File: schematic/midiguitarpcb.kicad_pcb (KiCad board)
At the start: 2 copper layers, 50 x 50 mm, 37 parts, among them CN1 NMJ6HCD2, J1 USB_C_Receptacle_USB2.0_16P, SW1 SW_Omron_B3FS, U1 AMS1117-3.3, U2 DIN-504D-M5, U3 STM32H743ZITx

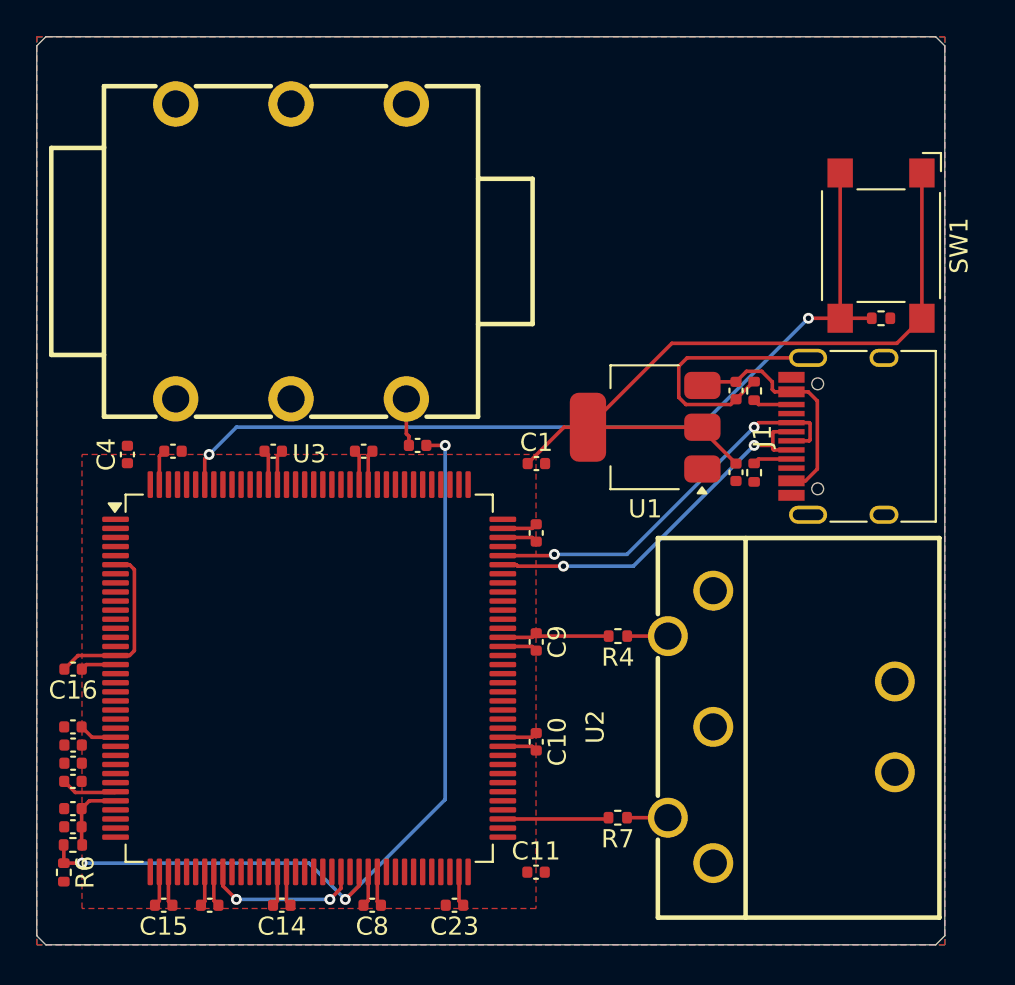
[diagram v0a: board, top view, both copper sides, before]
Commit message: wip working but noisy
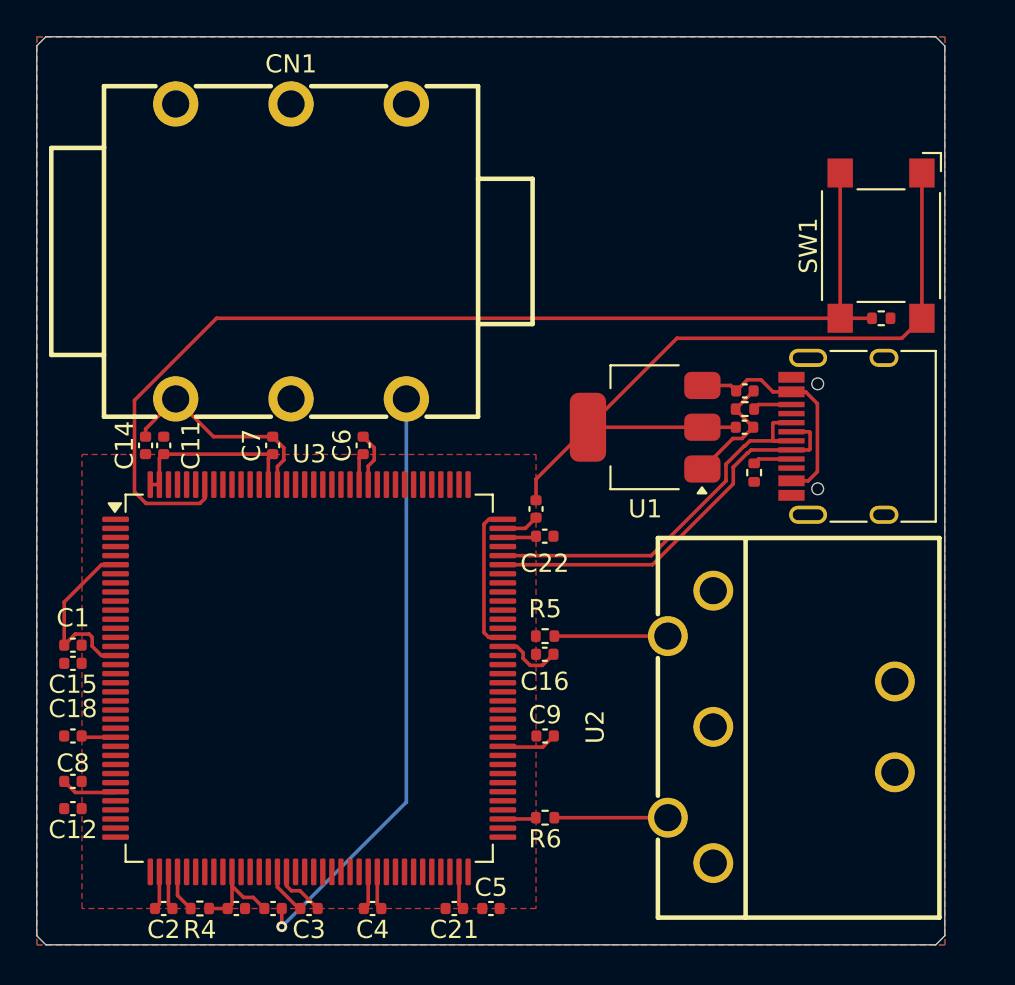
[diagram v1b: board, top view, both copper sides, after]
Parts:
- removed C23, C24: 2.2uF, Capacitor_SMD:C_0402_1005Metric
- removed R7: 10, Resistor_SMD:R_0402_1005Metric
- C19: value 47pF -> 1uF
- C20: value 100nF -> 100pF
- C21: value 1uF -> 2.2uF
- C22: value 100nF -> 2.2uF
- R4: value 33 -> 100K
- R5: value 100K -> 33
- R6: value 100K -> 10
- moved C11 31.2 mm to (57.0, 72.5), turned to 90 degrees
- moved C5 30.7 mm to (75.0, 98.0)
- moved R5 28.4 mm to (78.0, 83.0), turned to 180 degrees
- moved C4 28.4 mm to (68.5, 98.0), turned to 180 degrees
- moved R4 27.5 mm to (59.0, 98.0)
- moved C1 27.4 mm to (52.0, 83.5), turned to 180 degrees
- moved R6 26.7 mm to (78.0, 93.0), turned to 180 degrees
- moved C14 26.4 mm to (56.0, 72.5), turned to 90 degrees
- moved C16 26.0 mm to (78.0, 84.0), turned to 0 degrees
- moved C21 21.5 mm to (73.0, 98.0)
- moved C8 17.8 mm to (52.0, 91.0)
- moved C3 15.8 mm to (65.0, 98.0)
- moved C15 14.2 mm to (52.0, 84.5)
- moved C10 12.8 mm to (77.5, 76.0)
- moved C20 10.5 mm to (61.0, 98.0)
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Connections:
- C19 pad 1: Net-(U3-PA7) -> Net-(U3-PB0)
- C19 pad 2: Net-(U3-PC4) -> Net-(CN1-T)
- C20 pad 1: Net-(U3-VREF+) -> GND
- C20 pad 2: GND -> Net-(U3-PB0)
- C21 pad 1: Net-(U3-VREF+) -> Net-(C21-Pad1)
- C22 pad 1: Net-(CN1-T) -> Net-(C22-Pad1)
- C22 pad 2: Net-(U3-PE9) -> GND
- R4 pad 1: Net-(R4-Pad1) -> Net-(U3-PB0)
- R4 pad 2: +3V3 -> Net-(U3-PA4)
- R5 pad 1: Net-(U3-PE9) -> Net-(R5-Pad1)
- R5 pad 2: Net-(U3-VREF+) -> +3V3
- R6 pad 1: Net-(U3-PE9) -> Net-(R6-Pad1)
- R6 pad 2: GND -> Net-(U3-PB14)
- U2 pad 4: Net-(R4-Pad1) -> Net-(R5-Pad1)
- U2 pad 5: Net-(R7-Pad1) -> Net-(R6-Pad1)
- U3 pad 106: Net-(C24-Pad1) -> Net-(C22-Pad1)
- U3 pad 32: Net-(U3-VREF+) -> unconnected-(U3-VREF+-Pad32)
- U3 pad 40: unconnected-(U3-PA4-Pad40) -> Net-(U3-PA4)
- U3 pad 43: Net-(U3-PA7) -> unconnected-(U3-PA7-Pad43)
- U3 pad 44: Net-(U3-PC4) -> unconnected-(U3-PC4-Pad44)
- U3 pad 45: Net-(U3-PC5) -> unconnected-(U3-PC5-Pad45)
- U3 pad 46: unconnected-(U3-PB0-Pad46) -> Net-(U3-PB0)
- U3 pad 58: Net-(U3-PC5) -> unconnected-(U3-PE7-Pad58)
- U3 pad 60: Net-(U3-PE9) -> unconnected-(U3-PE9-Pad60)
- U3 pad 71: Net-(C23-Pad1) -> Net-(C21-Pad1)
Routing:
- net Net-(U3-PE9): track 47.5 -> 0.00 mm, vias 3 -> 0
- net Net-(CN1-T): track 2.62 -> 32.9 mm, vias 0 -> 1
- net Net-(U3-BOOT0): track 49.4 -> 60.5 mm, vias 2 -> 0
- net Net-(U3-PC5): track 8.74 -> 0.00 mm, vias 2 -> 0
- net GND: track 42.3 -> 50.2 mm
- net Net-(R6-Pad1): track 0.00 -> 6.25 mm
- net Net-(R5-Pad1): track 0.00 -> 6.25 mm
- net Net-(U3-PB0): track 0.00 -> 6.20 mm
- net +3V3: track 63.6 -> 69.5 mm
- net Net-(U3-VREF+): track 4.06 -> 0.00 mm
- net Net-(U3-PB14): track 5.85 -> 1.85 mm
- net Net-(U3-PA4): track 0.00 -> 2.32 mm
- net Net-(R7-Pad1): track 2.25 -> 0.00 mm
- net Net-(R4-Pad1): track 2.24 -> 0.00 mm
- net Net-(C21-Pad1): track 0.00 -> 2.11 mm
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
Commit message: redo pcb
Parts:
- added FB1: FerriteBead, Inductor_SMD:L_0805_2012Metric, F.Cu at (56.9, 23.0)
- added FB2: FerriteBead, Inductor_SMD:L_0805_2012Metric, F.Cu at (87.0, 33.5)
- added FB3: FerriteBead, Inductor_SMD:L_0805_2012Metric, F.Cu at (87.0, 43.5)
- added R7: 100K, Resistor_SMD:R_0805_2012Metric, F.Cu at (42.9, 36.0)
- added R8: 100K, Resistor_SMD:R_0805_2012Metric, F.Cu at (50.9, 36.0)
- added R9: 0, Resistor_SMD:R_0805_2012Metric, F.Cu at (63.9, 27.0)
- C1, C4, C9: value 100nF -> 1uF; footprint Capacitor_SMD:C_0402_1005Metric -> Capacitor_SMD:C_0805_2012Metric
- C10: value 100nF -> 10uF; footprint Capacitor_SMD:C_0402_1005Metric -> Capacitor_SMD:C_0805_2012Metric
- C11: value 100nF -> 100pF; footprint Capacitor_SMD:C_0402_1005Metric -> Capacitor_SMD:C_0805_2012Metric
- C12: value 4.7uF -> 100nF; footprint Capacitor_SMD:C_0402_1005Metric -> Capacitor_SMD:C_0805_2012Metric
- C13: value 10uF -> 1uF; footprint Capacitor_SMD:C_0402_1005Metric -> Capacitor_SMD:C_0805_2012Metric
- C14, C16: value 100nF -> 2.2uF; footprint Capacitor_SMD:C_0402_1005Metric -> Capacitor_SMD:C_0805_2012Metric
- C15, C18, C2, C3, C5, C6, C7: footprint Capacitor_SMD:C_0402_1005Metric -> Capacitor_SMD:C_0805_2012Metric
- C17: value 10uF -> 100nF; footprint Capacitor_SMD:C_0402_1005Metric -> Capacitor_SMD:C_0805_2012Metric
- C19: value 1uF -> 100nF; footprint Capacitor_SMD:C_0402_1005Metric -> Capacitor_SMD:C_0805_2012Metric
- C20: value 100pF -> 100nF; footprint Capacitor_SMD:C_0402_1005Metric -> Capacitor_SMD:C_0805_2012Metric
- C21: value 2.2uF -> 100nF; footprint Capacitor_SMD:C_0402_1005Metric -> Capacitor_SMD:C_0805_2012Metric
- C22: value 2.2uF -> 4.7uF; footprint Capacitor_SMD:C_0402_1005Metric -> Capacitor_SMD:C_0805_2012Metric
- C8: value 1uF -> 10uF; footprint Capacitor_SMD:C_0402_1005Metric -> Capacitor_SMD:C_0805_2012Metric
- R1: value 10K -> 33; footprint Resistor_SMD:R_0402_1005Metric -> Resistor_SMD:R_0805_2012Metric
- R2: value 5.1K -> 10K; footprint Resistor_SMD:R_0402_1005Metric -> Resistor_SMD:R_0805_2012Metric
- R3: value 5.1K -> 10; footprint Resistor_SMD:R_0402_1005Metric -> Resistor_SMD:R_0805_2012Metric
- R4: value 100K -> 5.1K; footprint Resistor_SMD:R_0402_1005Metric -> Resistor_SMD:R_0805_2012Metric
- R5: value 33 -> 5.1K; footprint Resistor_SMD:R_0402_1005Metric -> Resistor_SMD:R_0805_2012Metric
- R6: value 10 -> 100K; footprint Resistor_SMD:R_0402_1005Metric -> Resistor_SMD:R_0805_2012Metric
- U1: value AMS1117-3.3 -> DIN-504D-M5; footprint Package_TO_SOT_SMD:SOT-223-3_TabPin2 -> din5:CONN-TH_DIN-504D-M5
- U2: value DIN-504D-M5 -> STM32H743VGTx; footprint din5:CONN-TH_DIN-504D-M5 -> Package_QFP:LQFP-100_14x14mm_P0.5mm
- U3: value STM32H743ZITx -> AMS1117-3.3; footprint Package_QFP:LQFP-144_20x20mm_P0.5mm -> Package_TO_SOT_SMD:SOT-223-3_TabPin2
- moved R4 85.0 mm to (94.0, 20.5)
- moved C8 78.5 mm to (90.3, 22.5), turned to 0 degrees
- moved C12 74.2 mm to (77.9, 23.0)
- moved C4 73.5 mm to (60.4, 25.0), turned to 0 degrees
- moved C3 73.0 mm to (64.0, 25.0)
- moved C5 72.5 mm to (60.4, 27.0)
- moved C21 71.2 mm to (67.4, 27.0)
- moved C2 71.0 mm to (56.9, 27.0)
- moved C20 69.4 mm to (71.9, 29.5), turned to 0 degrees
- moved C19 69.1 mm to (53.9, 29.5)
- moved U3 65.4 mm to (84.2, 22.8), turned to 180 degrees
- moved R6 64.0 mm to (48.9, 36.0), turned to -90 degrees
- moved C9 62.1 mm to (44.9, 36.0), turned to 90 degrees
- moved R5 61.1 mm to (93.9, 24.0)
- moved C1 58.7 mm to (56.9, 25.0)
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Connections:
- C1 pad 1: +3V3 -> Net-(U2-VDDA)
- C1 pad 2: GND -> GNDA
- C11 pad 1: +3V3 -> Net-(U2-PC4)
- C11 pad 2: GND -> Net-(U2-PA7)
- C13 pad 1: VBUS -> Net-(CN1-T)
- C13 pad 2: GND -> Net-(U2-PC5)
- C14 pad 1: +3V3 -> Net-(C14-Pad1)
- C16 pad 1: +3V3 -> Net-(C16-Pad1)
- C18 pad 1: Net-(U3-NRST) -> +3V3
- C19 pad 1: Net-(U3-PB0) -> +3V3
- C19 pad 2: Net-(CN1-T) -> GND
- C2 pad 1: +3V3 -> Net-(U2-VDDA)
- C2 pad 2: GND -> GNDA
- C20 pad 1: GND -> +3V3
- C20 pad 2: Net-(U3-PB0) -> GND
- C21 pad 1: Net-(C21-Pad1) -> +3V3
- C22 pad 1: Net-(C22-Pad1) -> +3V3
- C3 pad 1: +3V3 -> GND
- C3 pad 2: GND -> Net-(U2-NRST)
- C4 pad 1: +3V3 -> VDDA
- C4 pad 2: GND -> GNDA
- C5 pad 1: +3V3 -> VDDA
- C5 pad 2: GND -> GNDA
- C6 pad 1: +3V3 -> Net-(U3-VI)
- C7 pad 1: +3V3 -> Net-(U2-PB0)
- C7 pad 2: GND -> GNDA
- C8 pad 1: +3V3 -> Net-(U3-VI)
- C9 pad 1: +3V3 -> Net-(U2-PB0)
- C9 pad 2: GND -> GNDA
- CN1 pad 3: GND -> GNDA
- CN1 pad 4: GND -> GNDA
- J1 pad A4: VBUS -> Net-(U3-VI)
- J1 pad A6: Net-(U3-PA12) -> Net-(U2-PA11)
- J1 pad A7: Net-(U3-PA11) -> Net-(U2-PA10)
- J1 pad A9: VBUS -> Net-(U3-VI)
- J1 pad B4: VBUS -> Net-(U3-VI)
- J1 pad B6: Net-(U3-PA12) -> Net-(U2-PA11)
- J1 pad B7: Net-(U3-PA11) -> Net-(U2-PA10)
- J1 pad B9: VBUS -> Net-(U3-VI)
- R1 pad 1: Net-(U3-BOOT0) -> Net-(FB2-Pad1)
- R1 pad 2: GND -> +3V3
- R2 pad 1: Net-(J1-CC2) -> Net-(U2-BOOT0)
- R3 pad 1: Net-(J1-CC1) -> Net-(FB3-Pad1)
- R3 pad 2: GND -> Net-(U2-PA9)
- R4 pad 1: Net-(U3-PB0) -> Net-(J1-CC2)
- R4 pad 2: Net-(U3-PA4) -> GND
- R5 pad 1: Net-(R5-Pad1) -> Net-(J1-CC1)
- R5 pad 2: +3V3 -> GND
- R6 pad 1: Net-(R6-Pad1) -> VDDA
- R6 pad 2: Net-(U3-PB14) -> Net-(U2-PB0)
- SW1 pad 2: Net-(U3-BOOT0) -> Net-(U2-BOOT0)
- U1 pad 1: GND -> unconnected-(U1-Pad1)
- U1 pad 2: +3V3 -> GND
- U1 pad 3: VBUS -> unconnected-(U1-Pad3)
- U2 pad 2: GND -> unconnected-(U2-PE3-Pad2)
- U2 pad 4: Net-(R5-Pad1) -> unconnected-(U2-PE5-Pad4)
- U2 pad 5: Net-(R6-Pad1) -> unconnected-(U2-PE6-Pad5)
- U2 pad 6: GND -> +3V3
- U2 pad 7: GND -> unconnected-(U2-PC13-Pad7)
- U3 pad 1: unconnected-(U3-PE2-Pad1) -> GND
- U3 pad 2: unconnected-(U3-PE3-Pad2) -> +3V3
- U3 pad 3: unconnected-(U3-PE4-Pad3) -> Net-(U3-VI)
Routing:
- net Net-(U3-BOOT0): track 60.5 -> 0.00 mm
- net Net-(U2-PA10): track 0.00 -> 44.9 mm, vias 0 -> 2
- net Net-(U2-PA11): track 0.00 -> 43.7 mm, vias 0 -> 2
- net GND: track 50.2 -> 81.8 mm, vias 0 -> 1
- net Net-(U3-PA11): track 22.0 -> 0.00 mm
- net Net-(U3-PA12): track 22.0 -> 0.00 mm
- net VDDA: track 0.00 -> 21.6 mm
- net Net-(U2-PA9): track 0.00 -> 21.1 mm
- net Net-(U3-VI): track 0.00 -> 19.5 mm
- net Net-(U2-BOOT0): track 0.00 -> 19.1 mm, vias 0 -> 2
- net GNDA: track 0.00 -> 17.2 mm
- net +3V3: track 69.5 -> 85.9 mm, vias 0 -> 2
- net Net-(U2-PB0): track 0.00 -> 13.2 mm
- net Net-(CN1-T): track 32.9 -> 20.2 mm, vias 1 -> 0
- net VBUS: track 12.6 -> 0.00 mm
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- added copper zone on B.Cu, net GNDA
- added copper zone on F.Cu, net GNDA
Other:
- board size 50 x 50 mm -> 90.5 x 36 mm

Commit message: wip about to put in mounting holes
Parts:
- added H1: MountingHole_Pad_MP, MountingHole:MountingHole_3.2mm_M3_Pad, F.Cu at (77.0, 62.1)
- added H2: MountingHole_Pad_MP, MountingHole:MountingHole_3.2mm_M3_Pad, F.Cu at (77.0, 70.1)
- added H3: MountingHole_Pad_MP, MountingHole:MountingHole_3.2mm_M3_Pad, F.Cu at (77.0, 78.0)
- added H4: MountingHole_Pad_MP, MountingHole:MountingHole_3.2mm_M3_Pad, F.Cu at (77.0, 86.0)
- added J1: Conn_ARM_SWD_TagConnect_TC2030, Connector:Tag-Connect_TC2030-IDC-FP_2x03_P1.27mm_Vertical, F.Cu at (46.5, 42.5)
- FB1, FB2, FB3: value FerriteBead -> 600@100MHz
- moved C16 0.50 mm to (68.8, 47.5)
- renumbered C13 to C12, C12 to C13, J1 to J2
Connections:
- net Net-(U2-PC5) renamed SWO
- J2 pad A6: Net-(U2-PA11) -> Net-(U2-PA12)
- J2 pad A7: Net-(U2-PA10) -> Net-(U2-PA11)
- J2 pad B6: Net-(U2-PA11) -> Net-(U2-PA12)
- J2 pad B7: Net-(U2-PA10) -> Net-(U2-PA11)
- U2 pad 69: Net-(U2-PA10) -> unconnected-(U2-PA10-Pad69)
- U2 pad 71: unconnected-(U2-PA12-Pad71) -> Net-(U2-PA12)
- U2 pad 72: unconnected-(U2-PA13-Pad72) -> SWDIO
- U2 pad 76: unconnected-(U2-PA14-Pad76) -> SWCLK
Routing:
- net Net-(U2-PA10): track 44.9 -> 0.00 mm, vias 2 -> 0
- net Net-(U2-PA12): track 0.00 -> 43.9 mm, vias 0 -> 2
- net SWCLK: track 0.00 -> 42.2 mm, vias 0 -> 2
- net Net-(J1-~{RESET}): track 5.75 -> 44.9 mm, vias 0 -> 2
- net SWDIO: track 0.00 -> 32.0 mm, vias 0 -> 2
- net GND: track 81.8 -> 112.1 mm, vias 1 -> 2
- net GNDA: track 17.2 -> 2.90 mm, vias 0 -> 1
- net SWO: track 4.57 -> 14.9 mm, vias 0 -> 2
- net +3V3: track 85.9 -> 91.7 mm
- net Net-(U2-PA11): track 43.7 -> 45.5 mm
- net Net-(U2-PA9): track 21.1 -> 21.8 mm
- net Net-(C16-Pad1): track 2.33 -> 2.83 mm

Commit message: wip about to put leds in
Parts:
- added D1: LED, LED_SMD:LED_0805_2012Metric, F.Cu at (66.7, 53.1)
- added D2: LED, LED_SMD:LED_0805_2012Metric, F.Cu at (66.7, 56.1)
- added R10: 1K, Resistor_SMD:R_0805_2012Metric, F.Cu at (71.1, 56.0)
- added R9: 1K, Resistor_SMD:R_0805_2012Metric, F.Cu at (71.1, 53.0)
- H1, H2, H3, H4: value MountingHole_Pad_MP -> MountingHole_Pad
- moved R4 62.0 mm to (35.6, 41.5)
- moved R5 61.5 mm to (35.6, 43.5)
- moved H1 56.2 mm to (41.0, 19.0)
- moved FB2 55.6 mm to (32.0, 41.5)
- moved H2 54.2 mm to (59.0, 19.0)
- moved R1 52.4 mm to (32.0, 43.5), turned to 0 degrees
- moved H3 50.2 mm to (41.0, 43.0)
- moved H4 46.6 mm to (59.0, 43.0)
- moved C18 45.7 mm to (34.0, 19.4), turned to 90 degrees
- moved R2 45.3 mm to (29.0, 42.5), turned to -90 degrees
- moved FB3 37.6 mm to (49.4, 43.5)
- moved C4 36.8 mm to (24.0, 19.4), turned to -90 degrees
- moved C5 35.2 mm to (26.0, 19.4), turned to -90 degrees
- moved R3 34.0 mm to (49.5, 41.0), turned to 0 degrees
- moved R6 31.6 mm to (22.0, 19.4)
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- renumbered R9 to R11
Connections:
- C12 pad 2: SWO -> Net-(U2-PC5)
- H1 pad 1: (no net) -> GND
- H2 pad 1: (no net) -> GND
- H3 pad 1: (no net) -> GND
- H4 pad 1: (no net) -> GND
- R8 pad 1: SWO -> Net-(U2-PC5)
- U2 pad 33: SWO -> Net-(U2-PC5)
- U2 pad 65: unconnected-(U2-PC8-Pad65) -> Net-(U2-PC8)
- U2 pad 66: unconnected-(U2-PC9-Pad66) -> Net-(U2-PC9)
- U2 pad 89: unconnected-(U2-PB3-Pad89) -> SWO
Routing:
- net GNDA: track 2.90 -> 58.6 mm
- net Net-(J2-CC1): track 2.57 -> 52.9 mm, vias 0 -> 2
- net Net-(J2-CC2): track 2.33 -> 50.8 mm, vias 0 -> 2
- net Net-(U2-BOOT0): track 18.8 -> 66.6 mm
- net Net-(FB2-Pad2): track 2.45 -> 47.7 mm, vias 0 -> 1
- net Net-(U2-PB0): track 13.2 -> 56.3 mm
- net +3V3: track 91.7 -> 127.8 mm, vias 2 -> 4
- net SWCLK: track 42.2 -> 13.0 mm, vias 2 -> 0
- net Net-(U2-PC5): track 0.00 -> 23.5 mm
- net Net-(FB3-Pad2): track 2.47 -> 24.1 mm, vias 0 -> 1
- net SWDIO: track 32.0 -> 10.9 mm, vias 2 -> 0
- net Net-(U2-PA9): track 21.8 -> 4.07 mm
- net GND: track 112.1 -> 128.1 mm, vias 2 -> 5
- net Net-(U2-VDDA): track 6.73 -> 22.1 mm
- net Net-(J1-~{RESET}): track 44.9 -> 33.4 mm
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- removed copper zone on F.Cu, net GND
- removed copper zone on B.Cu, net GNDA
- removed copper zone on F.Cu, net GNDA
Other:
- board size 90.5 x 36 mm -> 70 x 32 mm

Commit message: skinny pcb
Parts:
- C1, C10, C11, C12, C13, C14, C15, C16, C17, C18, C19, C2, C20, C21, C22, C3, C4, C5, C6, C7, C8, C9: footprint Capacitor_SMD:C_0805_2012Metric -> Capacitor_SMD:C_0603_1608Metric
- D1, D2: footprint LED_SMD:LED_0805_2012Metric -> LED_SMD:LED_0603_1608Metric
- FB1, FB2, FB3: footprint Inductor_SMD:L_0805_2012Metric -> Inductor_SMD:L_0603_1608Metric
- R1, R10, R11, R2, R3, R4, R5, R6, R7, R8, R9: footprint Resistor_SMD:R_0805_2012Metric -> Resistor_SMD:R_0603_1608Metric
- moved R10 40.7 mm to (53.0, 19.5), turned to -90 degrees
- moved R9 38.8 mm to (51.5, 19.5), turned to -90 degrees
- moved D2 35.6 mm to (66.3, 20.5), turned to 180 degrees
- moved FB2 35.5 mm to (67.5, 42.3), turned to 90 degrees
- moved D1 34.6 mm to (66.3, 18.5), turned to 180 degrees
- moved R1 33.5 mm to (65.5, 42.3), turned to 90 degrees
- moved C3 31.8 mm to (45.5, 19.6), turned to -90 degrees
- moved C22 26.7 mm to (50.0, 19.5), turned to 90 degrees
- moved C13 25.1 mm to (63.5, 42.3), turned to -90 degrees
- moved C19 24.4 mm to (48.5, 19.5), turned to 90 degrees
- moved R6 23.2 mm to (24.5, 42.5), turned to 90 degrees
- moved R2 21.0 mm to (50.0, 42.3)
- moved C10 20.0 mm to (45.5, 42.4)
- moved C21 15.8 mm to (60.0, 28.5)
- moved C18 13.0 mm to (47.0, 19.5)
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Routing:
- net +3V3: track 127.8 -> 14.9 mm, vias 4 -> 0
- net Net-(FB2-Pad2): track 47.7 -> 15.5 mm, vias 1 -> 0
- net Net-(U2-PB0): track 56.3 -> 26.4 mm
- net GND: track 128.1 -> 100.1 mm
- net Net-(U2-PC8): track 0.00 -> 25.1 mm, vias 0 -> 2
- net Net-(U2-PC9): track 0.00 -> 23.7 mm, vias 0 -> 2
- net VDDA: track 31.6 -> 53.8 mm
- net Net-(D1-A): track 0.00 -> 18.3 mm, vias 0 -> 2
- net Net-(J1-~{RESET}): track 33.4 -> 51.1 mm
- net Net-(D2-A): track 0.00 -> 15.0 mm, vias 0 -> 2
- net Net-(U3-VI): track 24.1 -> 38.5 mm, vias 0 -> 2
- net Net-(U2-BOOT0): track 66.6 -> 52.6 mm, vias 2 -> 3
- net Net-(J2-CC1): track 52.9 -> 39.2 mm
- net Net-(U2-PC5): track 23.5 -> 36.6 mm
- net Net-(J2-CC2): track 50.8 -> 40.3 mm
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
